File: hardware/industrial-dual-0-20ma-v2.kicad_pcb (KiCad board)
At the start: 2 copper layers, 40 x 40 mm, 41 parts, among them P1 CON-SENSOR2, P2 DEBUG, P3 BOOT, P4 P-PWR-8GN, Q1 FDN5630, U1 XMC1XXX24, U3 MCP3423, U4 DRILL, U5 DRILL, U6 DRILL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

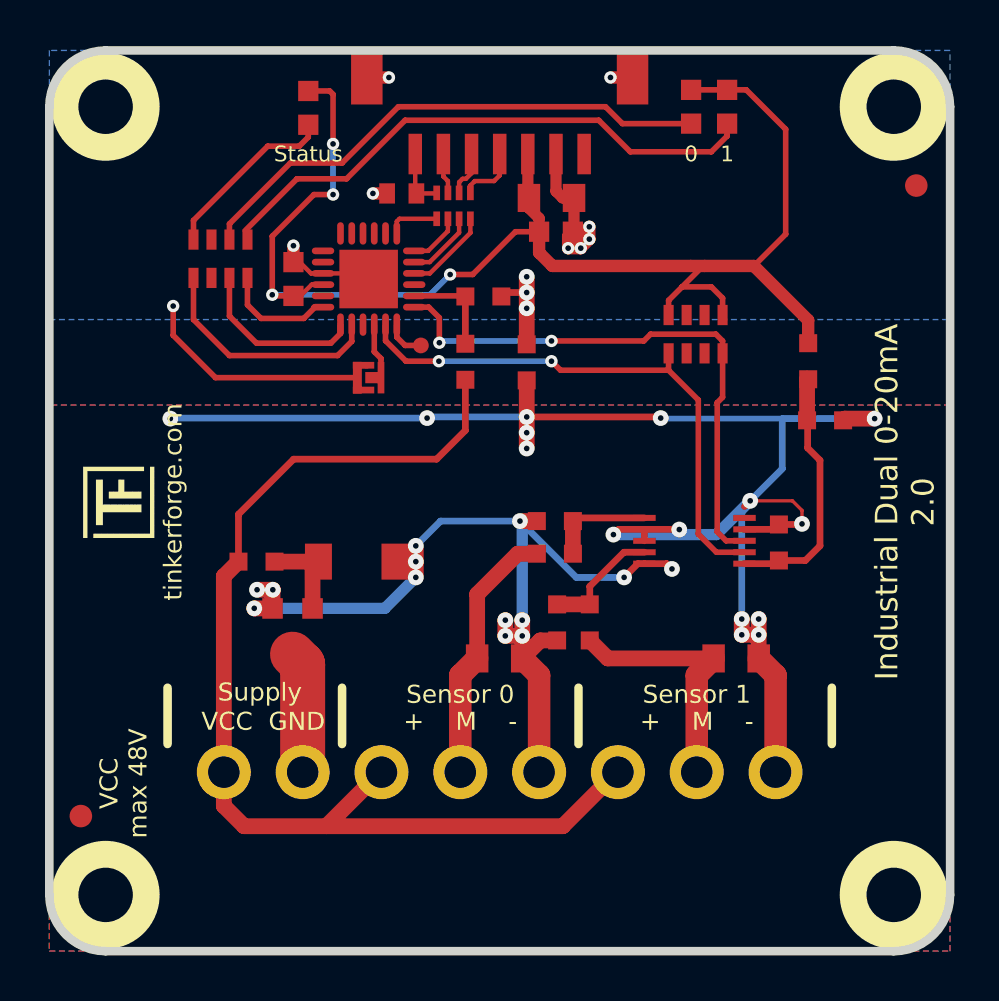
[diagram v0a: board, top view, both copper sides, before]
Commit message: Change footprints to x0402F/x0603F
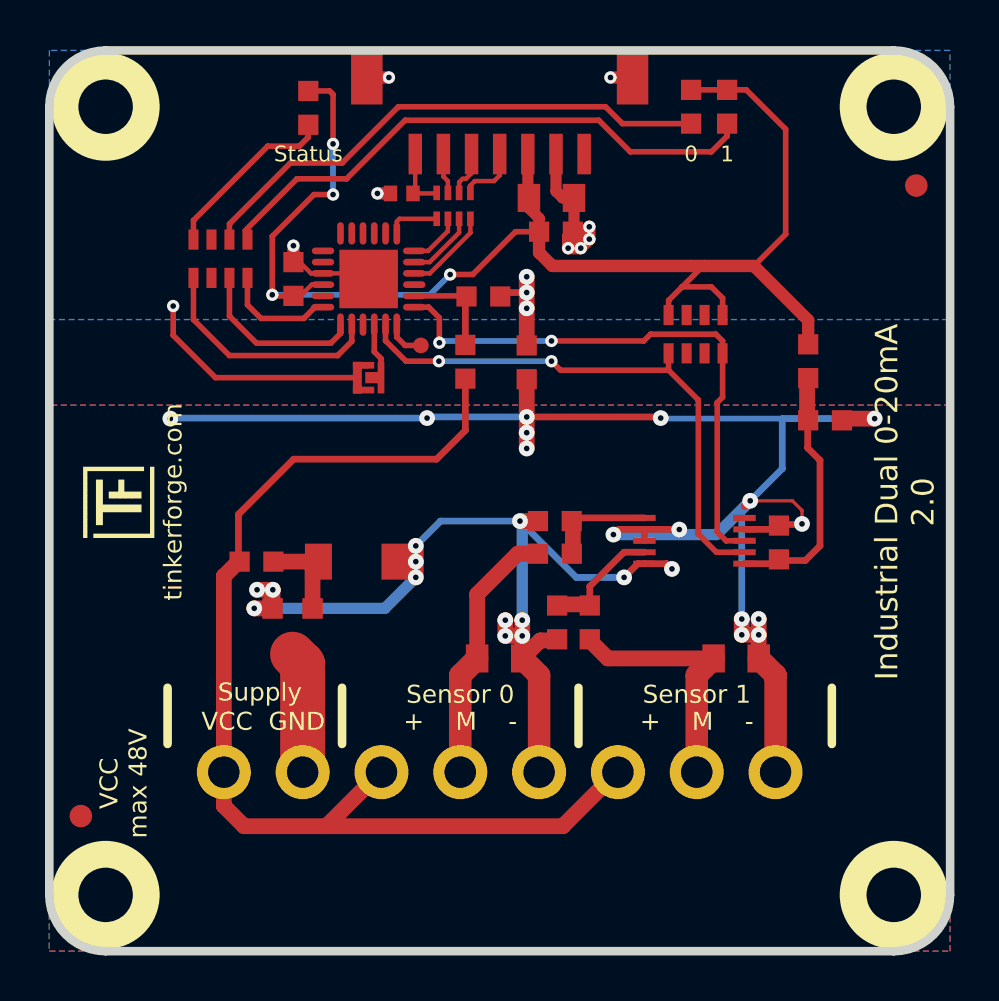
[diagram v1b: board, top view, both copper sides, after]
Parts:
- C2, C4, C5, C6, FB1, FB2: footprint kicad-libraries:C0603 -> kicad-libraries:C0603F
- C3: footprint kicad-libraries:C0402E -> kicad-libraries:C0402F
- R1, R2, R4, R5, R8: footprint kicad-libraries:R0603 -> kicad-libraries:R0603F
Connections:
- P1 pad 1: (no net) -> Net-(P1-Pad1)
- RP101 pad 2: (no net) -> Net-(RP101-Pad2)
- RP101 pad 3: (no net) -> Net-(RP101-Pad3)
- RP101 pad 6: (no net) -> Net-(RP101-Pad6)
- RP101 pad 7: (no net) -> Net-(RP101-Pad7)
- RP2 pad 2: (no net) -> Net-(RP2-Pad2)
- RP2 pad 7: (no net) -> Net-(RP2-Pad7)
- U1 pad 11: (no net) -> Net-(U1-Pad11)
- U1 pad 15: (no net) -> Net-(U1-Pad15)
- U1 pad 2: (no net) -> Net-(U1-Pad2)
- U1 pad 21: (no net) -> Net-(U1-Pad21)
- U1 pad 3: (no net) -> Net-(U1-Pad3)
- U1 pad 4: (no net) -> Net-(U1-Pad4)
- U1 pad 5: (no net) -> Net-(U1-Pad5)
- U1 pad 6: (no net) -> Net-(U1-Pad6)
- U1 pad 7: (no net) -> Net-(U1-Pad7)
- U1 pad 8: (no net) -> Net-(U1-Pad8)
- U3 pad 10: (no net) -> Net-(U3-Pad10)

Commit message: specify processor
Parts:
- U1: value XMC1XXX24 -> XMC11XX24
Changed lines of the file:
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@@
-(kicad_pcb (version 4) (host pcbnew 4.0.2+dfsg1-stable)
+(kicad_pcb (version 4) (host pcbnew 4.0.7-e2-6376~61~ubuntu18.04.1)
   (general
     (links 82)
     (no_connects 0)
-    (area 97.609659 37.858699 137.993121 78.242161)
+    (area 96.945139 37.195139 280.14286 166.44)
     (thickness 1.6002)
     (drawings 25)
@@
   )
   (setup
-    (last_trace_width 0.55)
+    (last_trace_width 0.14986)
     (user_trace_width 0.2)
     (user_trace_width 0.25)
@@
       (effects (font (size 0.3 0.3) (thickness 0.075)))
     )
-    (fp_text value XMC1XXX24 (at 0 0.8 270) (layer F.Fab)
+    (fp_text value XMC11XX24 (at 0 0.8 270) (layer F.Fab)
       (effects (font (size 0.3 0.3) (thickness 0.075)))
     )
@@
   (segment (start 119 54.325) (end 119 52.6751) (width 0.70104) (layer Front) (net 3))
   (segment (start 114.075 60.75) (end 113.12426 60.75) (width 0.70104) (layer Front) (net 3))
-  (segment (start 112.95 44.4) (end 112.37 44.4) (width 0.55) (layer Front) (net 4) (status 400000))
+  (segment (start 112.95 44.4) (end 112.37 44.4) (width 0.55) (layer Front) (net 4))
   (via (at 112.37 44.4) (size 0.55) (drill 0.25) (layers Front Back) (net 4))
   (segment (start 111.48 52.58) (end 105.18 52.58) (width 0.25) (layer Front) (net 4))

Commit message: specify processor as XMC1100
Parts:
- U1: value XMC11XX24 -> XMC1100

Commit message: Data Cleanup
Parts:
- moved R4 0.11 mm to (120.2, 60.3)
- moved R1 0.11 mm to (117.0, 48.9)
- moved U1 0.10 mm to (112.0, 48.1)
- moved C4 0.10 mm to (130.2, 60.0)
- moved P4 0.10 mm to (117.8, 70.0)
- moved RP2 0.10 mm to (105.4, 47.2)
- moved C2 0.09 mm to (132.2, 54.4)
- moved P3 0.08 mm to (112.0, 52.5)
- moved R2 0.08 mm to (116.3, 51.8)
- moved C6 0.07 mm to (120.4, 63.4)
- moved C5 0.07 mm to (120.3, 58.9)
- moved RP1 0.07 mm to (115.7, 44.9)
- moved D1 0.07 mm to (111.4, 60.7)
- moved U3 0.06 mm to (126.5, 59.8)
- moved FB1 0.05 mm to (131.5, 51.8)
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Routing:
- net AGND: track 111.5 -> 115.2 mm
- net GND: track 37.5 -> 36.6 mm
- net Net-(RP2-Pad6): track 8.04 -> 7.37 mm
- net Net-(RP2-Pad5): track 5.72 -> 5.05 mm
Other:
- net class Default removed
- board text added: "Copyright Tinkerforge GmbH 2023. This documentation describes Open Hardware and is licensed under the CERN OHL v. 1.1. You may redistribute and modify this documentation under the terms of the CERN OHL v.1.1. (http://ohwr.org/cernohl). This documentation is distributed WITHOUT ANY EXPRESS OR IMPLIED WARRANTY, INCLUDING OF MERCHANTABILITY, SATISFACTORY QUALITY AND FITNESS FOR A PARTICULAR PURPOSE.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"
- board text removed: "Copyright Tinkerforge GmbH 2018. This documentation describes Open Hardware and is licensed under the CERN OHL v. 1.1. You may redistribute and modify this documentation under the terms of the CERN OHL v.1.1. (http://ohwr.org/cernohl). This documentation is distributed WITHOUT ANY EXPRESS OR IMPLIED WARRANTY, INCLUDING OF MERCHANTABILITY, SATISFACTORY QUALITY AND FITNESS FOR A PARTICULAR PURPOSE.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"
